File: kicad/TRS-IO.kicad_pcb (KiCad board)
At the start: 2 copper layers, 81.3 x 59.9 mm, 11 parts, among them J1 TRS-80, J2 Conn_01x19, J3 Conn_01x19, Q1 2N7000, Q2 2N7000, Q3 2N7000, SW1 SW_Push, U1 GAL16V8, U2 74LS245, U3 74LS245

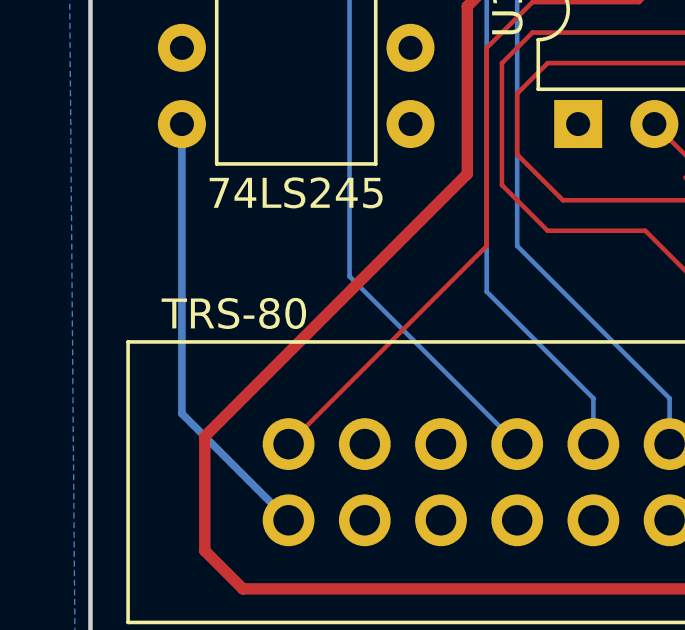
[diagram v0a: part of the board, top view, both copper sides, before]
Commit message: Create proper kicad symbol for TRS-80 IO port
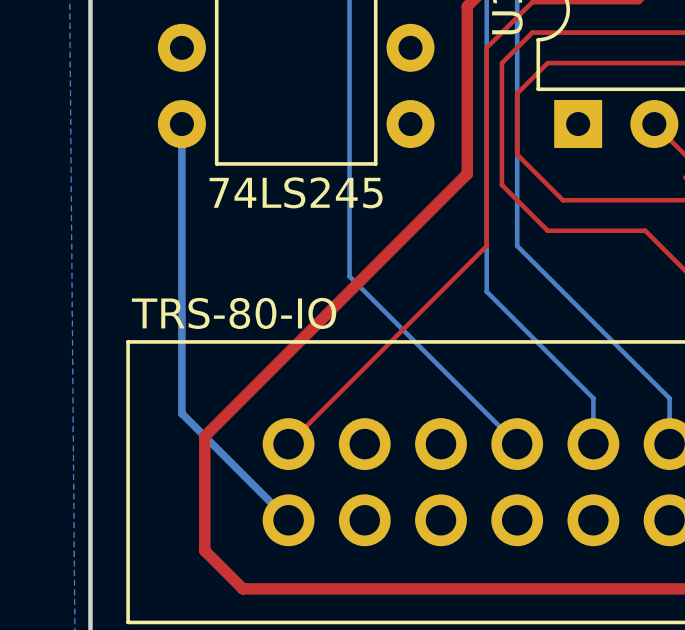
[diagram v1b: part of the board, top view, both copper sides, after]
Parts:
- J1: value TRS-80 -> TRS-80-IO
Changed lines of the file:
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@@
       (effects (font (size 1 1) (thickness 0.15)))
     )
-    (fp_text value TRS-80 (at -4.318 62.738) (layer F.SilkS)
+    (fp_text value TRS-80-IO (at -4.318 62.738) (layer F.SilkS)
       (effects (font (size 1 1) (thickness 0.15)))
     )
